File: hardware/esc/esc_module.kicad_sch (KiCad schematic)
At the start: 31 parts, among them U3 STDRIVE101, U4 STM32L431KBU6

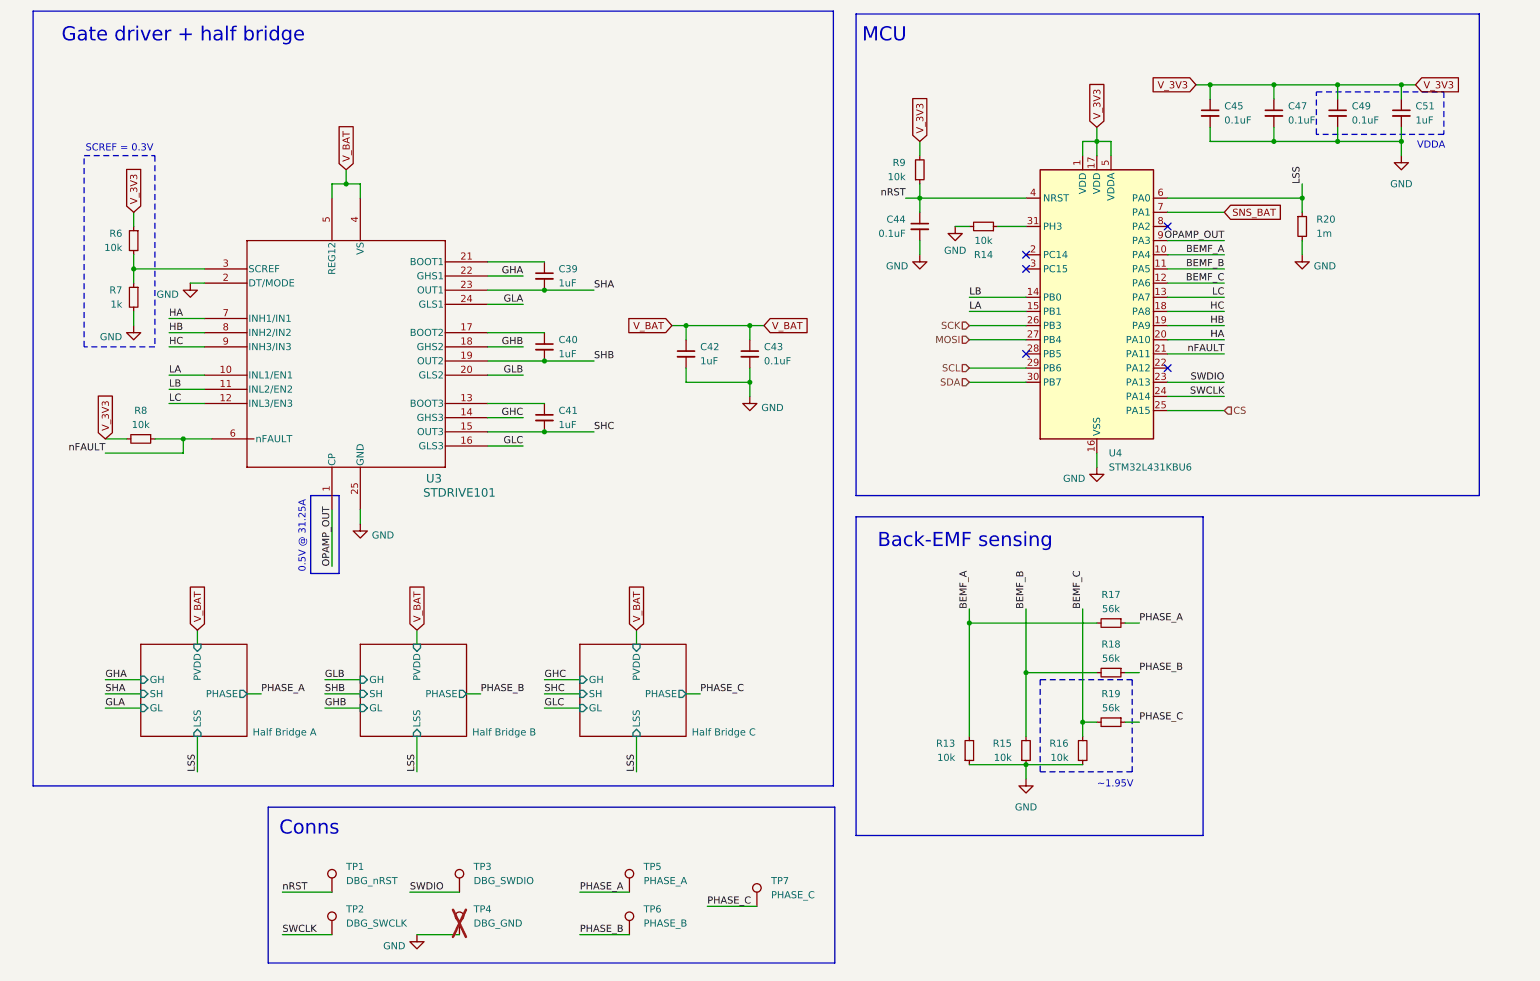
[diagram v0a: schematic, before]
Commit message: h/feat: preliminary rev 2 schematic
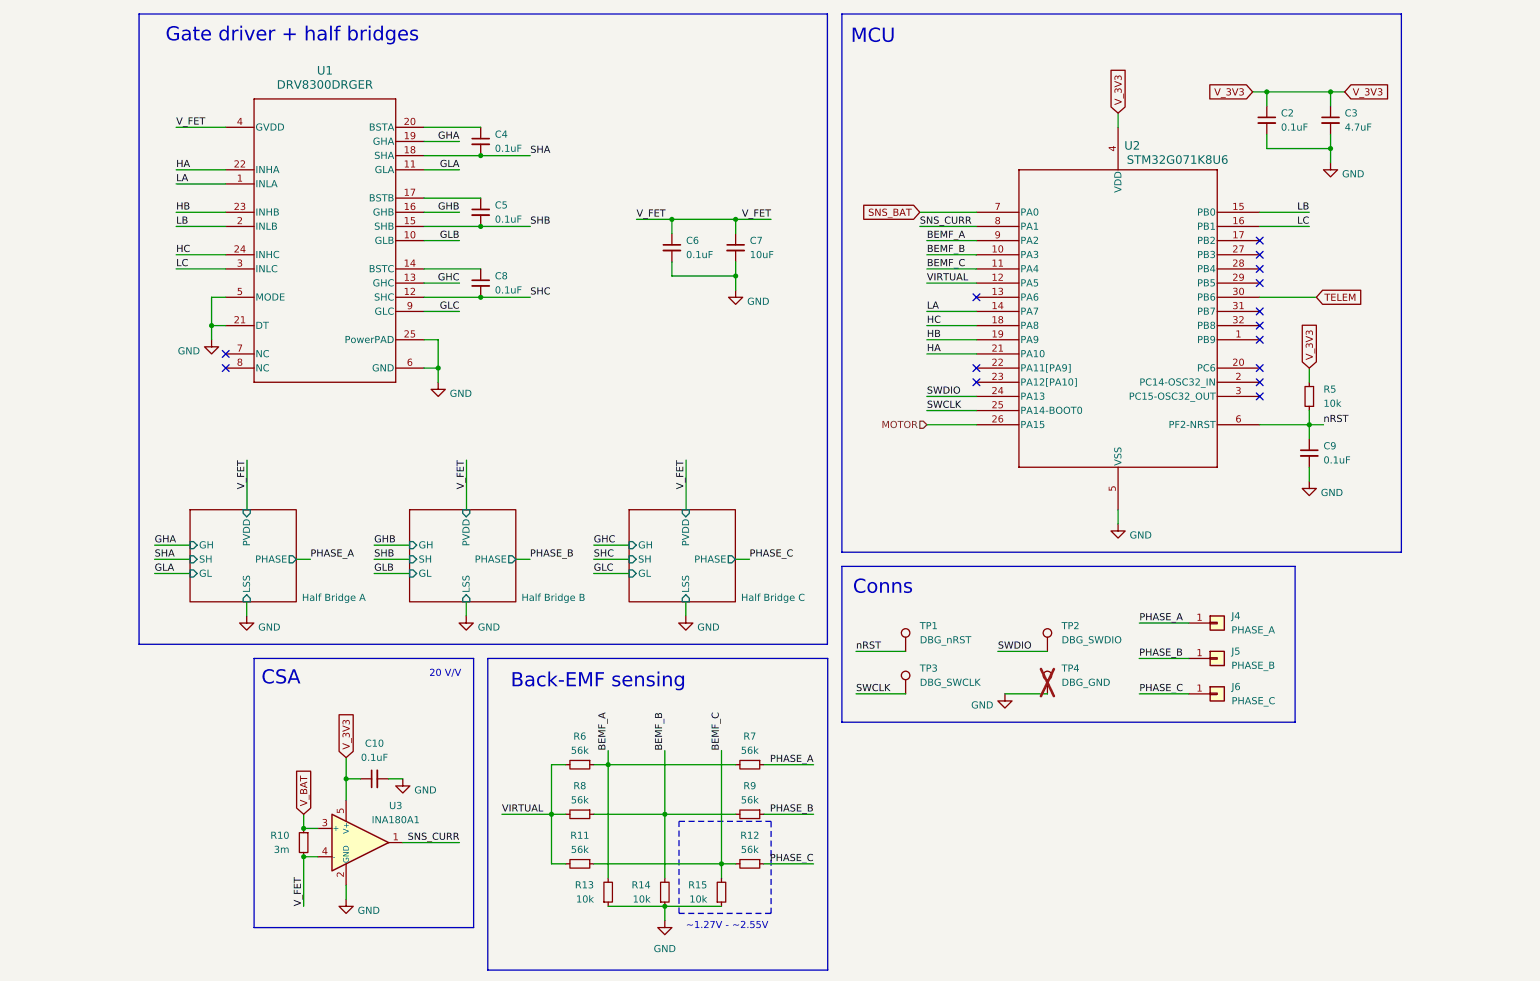
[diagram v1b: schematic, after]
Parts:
- removed C39, C40, C41, C51: 1uF, Capacitor_SMD:C_0402_1005Metric, symbol Device:C_Small
- removed C44, C45, C47, C49: 0.1uF, Capacitor_SMD:C_0402_1005Metric, symbol Device:C_Small
- removed R14, R9: 10k, Resistor_SMD:R_0402_1005Metric, symbol Device:R_Small
- removed R20: 1m, Resistor_SMD:R_0805_2012Metric, symbol Device:R_Small
- removed R7: 1k, Resistor_SMD:R_0402_1005Metric, symbol Device:R_Small
- removed TP5: PHASE_A, Stratus:Phase_Pad_3x3_D1.5, symbol Connector:TestPoint
- removed TP6: PHASE_B, Stratus:Phase_Pad_3x3_D1.5, symbol Connector:TestPoint
- removed TP7: PHASE_C, Stratus:Phase_Pad_3x3_D1.5, symbol Connector:TestPoint
- removed U3: STDRIVE101, Stratus:STDRIVE101, symbol STDRIVE101:STDRIVE101
- removed U4: STM32L431KBU6, Stratus:STM32L431KBU6, symbol MCU_ST_STM32L4:STM32L431KBUx
- added C10, C2, C4, C5, C8, C9: 0.1uF, Capacitor_SMD:C_0402_1005Metric, symbol Device:C_Small
- added C3: 4.7uF, Capacitor_SMD:C_0402_1005Metric, symbol Device:C_Small
- added J4: PHASE_A, Stratus:Phase_Pad_3x3_D1.5, symbol Connector_Generic:Conn_01x01
- added J5: PHASE_B, Stratus:Phase_Pad_3x3_D1.5, symbol Connector_Generic:Conn_01x01
- added J6: PHASE_C, Stratus:Phase_Pad_3x3_D1.5, symbol Connector_Generic:Conn_01x01
- added R10: 3m, Resistor_SMD:R_2512_6332Metric, symbol Device:R_Small
- added R11: 56k, Resistor_SMD:R_0402_1005Metric, symbol Device:R_Small
- added R5: 10k, Resistor_SMD:R_0402_1005Metric, symbol Device:R_Small
- added U1: DRV8300DRGER, DRV8300DRGER:DRV8300DRGER, symbol DRV8300DRGER:DRV8300DRGER
- added U2: STM32G071K8U6, STM32G071K8U6:STM32G071K8U6, symbol STM32G071K8U6:STM32G071K8U6
- added U3: INA180A1, Package_TO_SOT_SMD:SOT-23-5, symbol Amplifier_Current:INA180A1
- C6: renamed from C42; value 1uF -> 0.1uF
- C7: renamed from C43; value 0.1uF -> 10uF; footprint Capacitor_SMD:C_0402_1005Metric -> Capacitor_SMD:C_0805_2012Metric
- R6, R8: value 10k -> 56k; Manufacturer_Part_Number RC0402FR-0710KL -> RC0402FR-0756KL
- renumbered R19 to R12, R15 to R14, R16 to R15, R17 to R7, R18 to R9, TP3 to TP2, TP2 to TP3
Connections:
- net nFAULT is gone; now on net BEMF_B: R8.1
- net BEMF_A: now also R6.1, U2.9 (PA2)
- net BEMF_B: now also U2.10 (PA3)
- net BEMF_C: now also R11.1, U2.11 (PA4)
- net GHA: now also U1.19 (GHA)
- net GHB: now also U1.16 (GHB)
- net GHC: now also U1.13 (GHC)
- net GLA: now also U1.11 (GLA)
- net GLB: now also U1.10 (GLB)
- net GLC: now also U1.9 (GLC)
- net GND: now also C10.2, C2.2, C3.2, C9.2, U1.21 (DT), U1.25 (PowerPAD), U1.5 (MODE), U1.6 (GND), U2.5 (VSS), U3.2 (GND)
- net HA: now also U1.22 (INHA), U2.21 (PA10)
- net HB: now also U1.23 (INHB), U2.19 (PA9)
- net HC: now also U1.24 (INHC), U2.18 (PA8)
- net LA: now also U1.1 (INLA), U2.14 (PA7)
- net LB: now also U1.2 (INLB), U2.15 (PB0)
- net LC: now also U1.3 (INLC), U2.16 (PB1)
- net PHASE_A: now also J4.1 (Pin_1)
- net PHASE_B: now also J5.1 (Pin_1)
- net PHASE_C: now also J6.1 (Pin_1)
- net SHA: now also C4.2, U1.18 (SHA)
- net SHB: now also C5.2, U1.15 (SHB)
- net SHC: now also C8.2, U1.12 (SHC)
- net SNS_BAT: now also U2.7 (PA0)
- net SWCLK: now also U2.25 (PA14-BOOT0)
- net SWDIO: now also U2.24 (PA13)
- net V_3V3: now also C10.1, C2.1, C3.1, R5.2, U2.4 (VDD), U3.5 (V+); no longer R6.1, R8.2
- net V_BAT: now also R10.1, U3.3 (+); no longer C6.1, C7.1
- net nRST: now also C9.1, R5.1, U2.6 (PF2-NRST)
- net VIRTUAL: now reaches R6.2
- net VIRTUAL: now also R8.2, R11.2, U2.12 (PA5)
- new net: C8.1, U1.14 (BSTC)
- new net: C5.1, U1.17 (BSTB)
- new net: C4.1, U1.20 (BSTA)
- new net MOTOR: U2.26 (PA15)
- new net SNS_CURR: U2.8 (PA1), U3.1
- new net TELEM: U2.30 (PB6)
- new net V_FET: C6.1, C7.1, R10.2, U1.4 (GVDD), U3.4 (-)
- no-connect marks 5 -> 15
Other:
- note added: "20 V/V"
- note added: "CSA"
- note added: "Gate driver + half bridges"
- note added: "~1.27V - ~2.55V"
- note removed: "0.5V @ 31.25A"
- note removed: "Gate driver + half bridge"
- note removed: "SCREF = 0.3V"
- note removed: "VDDA"
- note removed: "~1.95V"
- moved on the sheet: C6, C7, R12, R13, R14, R15, R7, R9, TP1, TP2, TP3, TP4

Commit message: chore: prep: footprints, 3d models, pcb
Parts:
- U1: footprint DRV8300DRGER:DRV8300DRGER -> Stratus:DRV8300DRGER
- U2: footprint STM32G071K8U6:STM32G071K8U6 -> Stratus:STM32G071K8U6
- U3: footprint Package_TO_SOT_SMD:SOT-23-5 -> Stratus:INA180A1IDBVR
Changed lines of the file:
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@@
 			)
 		)
-		(property "Footprint" "DRV8300DRGER:DRV8300DRGER"
+		(property "Footprint" "Stratus:DRV8300DRGER"
 			(at 49.53 35.56 0)
 			(hide yes)
@@
 			)
 		)
-		(property "Footprint" "STM32G071K8U6:STM32G071K8U6"
+		(property "Footprint" "Stratus:STM32G071K8U6"
 			(at 184.15 50.8 0)
 			(hide yes)
@@
 			)
 		)
-		(property "Footprint" "Package_TO_SOT_SMD:SOT-23-5"
+		(property "Footprint" "Stratus:INA180A1IDBVR"
 			(at 73.66 185.42 0)
 			(hide yes)

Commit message: h/feat: gate drive routing + prelim layout
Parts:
- C10, C2, C3, C4, C5, C6, C8, C9: footprint Capacitor_SMD:C_0402_1005Metric -> Stratus:C_0402
- R11, R12, R13, R14, R15, R5, R6, R7, R8, R9: footprint Resistor_SMD:R_0402_1005Metric -> Stratus:R_0402
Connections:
- net LA: now also U2.16 (PB1); no longer U2.14 (PA7)
- net LC: now also U2.14 (PA7); no longer U2.16 (PB1)
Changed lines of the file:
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@@
 	(wire
 		(pts
+			(xy 53.34 95.25) (xy 53.34 104.14)
+		)
+		(stroke
+			(width 0)
+			(type default)
+		)
+	)
+	(wire
+		(pts
 			(xy 85.09 40.64) (xy 95.25 40.64)
 		)
@@
 	(wire
 		(pts
-			(xy 53.34 95.25) (xy 53.34 104.14)
-		)
-		(stroke
-			(width 0)
-			(type default)
-		)
-	)
-	(wire
-		(pts
 			(xy 85.09 55.88) (xy 91.44 55.88)
 		)
@@
 		)
 	)
-	(label "LA"
+	(label "LC"
 		(at 175.26 68.58 0)
 		(effects
@@
 		)
 	)
-	(label "LC"
+	(label "LA"
 		(at 243.84 53.34 180)
 		(effects
@@
 			)
 		)
-		(property "Footprint" "Resistor_SMD:R_0402_1005Metric"
+		(property "Footprint" "Stratus:R_0402"
 			(at 143.51 167.64 0)
 			(hide yes)
@@
 			)
 		)
-		(property "Footprint" "Capacitor_SMD:C_0402_1005Metric"
+		(property "Footprint" "Stratus:C_0402"
 			(at 243.84 93.98 0)
 			(hide yes)
@@
 			)
 		)
-		(property "Footprint" "Resistor_SMD:R_0402_1005Metric"
+		(property "Footprint" "Stratus:R_0402"
 			(at 118.11 172.72 0)
 			(hide yes)
@@
 			)
 		)
-		(property "Footprint" "Resistor_SMD:R_0402_1005Metric"
+		(property "Footprint" "Stratus:R_0402"
 			(at 138.43 172.72 0)
 			(hide yes)
@@
 			)
 		)
-		(property "Footprint" "Capacitor_SMD:C_0402_1005Metric"
+		(property "Footprint" "Stratus:C_0402"
 			(at 247.65 34.29 0)
 			(hide yes)
@@
 			)
 		)
-		(property "Footprint" "Resistor_SMD:R_0402_1005Metric"
+		(property "Footprint" "Stratus:R_0402"
 			(at 113.03 158.75 0)
 			(hide yes)
@@
 			)
 		)
-		(property "Footprint" "Resistor_SMD:R_0402_1005Metric"
+		(property "Footprint" "Stratus:R_0402"
 			(at 113.03 149.86 0)
 			(hide yes)
@@
 			)
 		)
-		(property "Footprint" "Capacitor_SMD:C_0402_1005Metric"
+		(property "Footprint" "Stratus:C_0402"
 			(at 129.54 57.15 0)
 			(hide yes)
@@
 			)
 		)
-		(property "Footprint" "Capacitor_SMD:C_0402_1005Metric"
+		(property "Footprint" "Stratus:C_0402"
 			(at 95.25 63.5 0)
 			(hide yes)
@@
 			)
 		)
-		(property "Footprint" "Resistor_SMD:R_0402_1005Metric"
+		(property "Footprint" "Stratus:R_0402"
 			(at 143.51 158.75 0)
 			(hide yes)
@@
 			)
 		)
-		(property "Footprint" "Resistor_SMD:R_0402_1005Metric"
+		(property "Footprint" "Stratus:R_0402"
 			(at 113.03 167.64 0)
 			(hide yes)
@@
 			)
 		)
-		(property "Footprint" "Resistor_SMD:R_0402_1005Metric"
+		(property "Footprint" "Stratus:R_0402"
 			(at 128.27 172.72 0)
 			(hide yes)
@@
 			)
 		)
-		(property "Footprint" "Capacitor_SMD:C_0402_1005Metric"
+		(property "Footprint" "Stratus:C_0402"
 			(at 95.25 50.8 0)
 			(hide yes)
@@
 			)
 		)
-		(property "Footprint" "Capacitor_SMD:C_0402_1005Metric"
+		(property "Footprint" "Stratus:C_0402"
 			(at 76.2 152.4 0)
 			(hide yes)
@@
 			)
 		)
-		(property "Footprint" "Capacitor_SMD:C_0402_1005Metric"
+		(property "Footprint" "Stratus:C_0402"
 			(at 95.25 38.1 0)
 			(hide yes)
@@
 			)
 		)
-		(property "Footprint" "Resistor_SMD:R_0402_1005Metric"
+		(property "Footprint" "Stratus:R_0402"
 			(at 143.51 149.86 0)
 			(hide yes)
@@
 			)
 		)
-		(property "Footprint" "Resistor_SMD:R_0402_1005Metric"
+		(property "Footprint" "Stratus:R_0402"
 			(at 243.84 83.82 0)
 			(hide yes)
@@
 			)
 		)
-		(property "Footprint" "Capacitor_SMD:C_0402_1005Metric"
+		(property "Footprint" "Stratus:C_0402"
 			(at 236.22 34.29 0)
 			(hide yes)
@@
 		)
 		(pin "PVDD" input
-			(at 53.2878 104.14 90)
+			(at 53.34 104.14 90)
 			(effects
 				(font
@@
 		)
 		(pin "PVDD" input
-			(at 132.0278 104.14 90)
+			(at 132.08 104.14 90)
 			(effects
 				(font
@@
 		)
 		(pin "PVDD" input
-			(at 92.6578 104.14 90)
+			(at 92.71 104.14 90)
 			(effects
 				(font

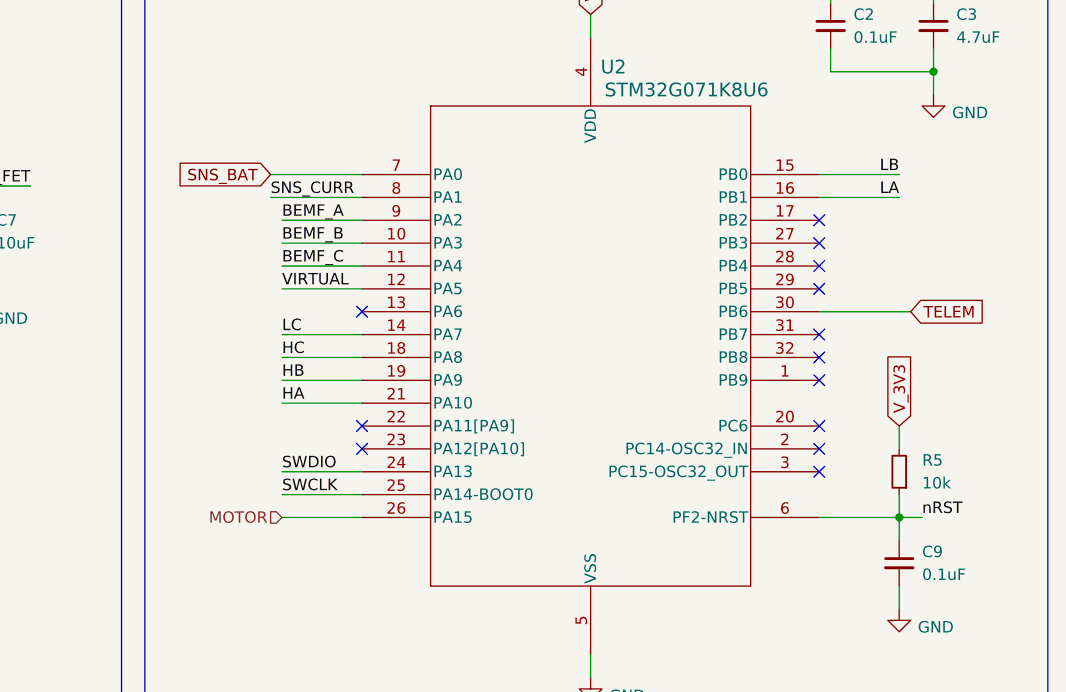
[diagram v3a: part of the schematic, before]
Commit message: h/fix: update schematic to better match AM32 hardware groups; further layout work
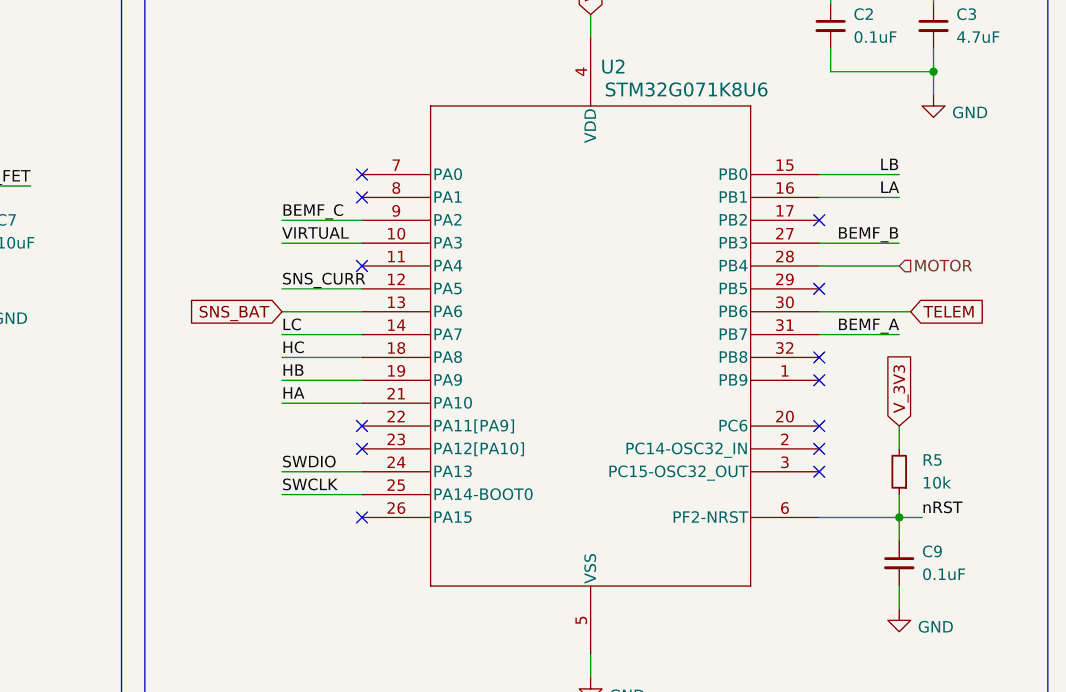
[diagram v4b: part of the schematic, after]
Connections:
- net BEMF_A: now also U2.31 (PB7); no longer U2.9 (PA2)
- net BEMF_B: now also U2.27 (PB3); no longer U2.10 (PA3)
- net BEMF_C: now also U2.9 (PA2); no longer U2.11 (PA4)
- net MOTOR: now also U2.28 (PB4); no longer U2.26 (PA15)
- net SNS_BAT: now also U2.13 (PA6); no longer U2.7 (PA0)
- net SNS_CURR: now also U2.12 (PA5); no longer U2.8 (PA1)
- net VIRTUAL: now also U2.10 (PA3); no longer U2.12 (PA5)
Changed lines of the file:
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@@
-	)
-	(no_connect
-		(at 234.95 58.42)
-	)
-	(no_connect
-		(at 184.15 66.04)
 	)
 	(no_connect
@@
 	)
 	(no_connect
+		(at 184.15 88.9)
+	)
+	(no_connect
+		(at 184.15 50.8)
+	)
+	(no_connect
 		(at 234.95 63.5)
 	)
@@
 	)
 	(no_connect
+		(at 184.15 53.34)
+	)
+	(no_connect
 		(at 184.15 81.28)
 	)
@@
 	)
 	(no_connect
-		(at 234.95 60.96)
-	)
-	(no_connect
 		(at 49.53 76.2)
 	)
@@
 	)
 	(no_connect
-		(at 234.95 68.58)
+		(at 184.15 60.96)
 	)
 	(no_connect
@@
 	(wire
 		(pts
+			(xy 175.26 66.04) (xy 184.15 66.04)
+		)
+		(stroke
+			(width 0)
+			(type default)
+		)
+	)
+	(wire
+		(pts
 			(xy 236.22 29.21) (xy 233.68 29.21)
 		)
@@
 	(wire
 		(pts
-			(xy 184.15 50.8) (xy 173.99 50.8)
-		)
-		(stroke
-			(width 0)
-			(type default)
-		)
-	)
-	(wire
-		(pts
 			(xy 53.2878 120.65) (xy 53.2878 123.19)
 		)
@@
 	(wire
 		(pts
-			(xy 184.15 53.34) (xy 173.99 53.34)
-		)
-		(stroke
-			(width 0)
-			(type default)
-		)
-	)
-	(wire
-		(pts
 			(xy 63.5 166.37) (xy 66.04 166.37)
 		)
@@
 	(wire
 		(pts
+			(xy 234.95 68.58) (xy 243.84 68.58)
+		)
+		(stroke
+			(width 0)
+			(type default)
+		)
+	)
+	(wire
+		(pts
 			(xy 40.64 45.72) (xy 49.53 45.72)
 		)
@@
 	(wire
 		(pts
+			(xy 234.95 58.42) (xy 243.84 58.42)
+		)
+		(stroke
+			(width 0)
+			(type default)
+		)
+	)
+	(wire
+		(pts
 			(xy 85.09 50.8) (xy 91.44 50.8)
 		)
@@
 	(wire
 		(pts
-			(xy 184.15 88.9) (xy 175.26 88.9)
-		)
-		(stroke
-			(width 0)
-			(type default)
-		)
-	)
-	(wire
-		(pts
 			(xy 99.06 158.75) (xy 107.95 158.75)
 		)
@@
 	(wire
 		(pts
+			(xy 234.95 60.96) (xy 243.84 60.96)
+		)
+		(stroke
+			(width 0)
+			(type default)
+		)
+	)
+	(wire
+		(pts
 			(xy 140.97 64.77) (xy 140.97 62.23)
-		)
-		(stroke
-			(width 0)
-			(type default)
-		)
-	)
-	(wire
-		(pts
-			(xy 184.15 60.96) (xy 175.26 60.96)
 		)
 		(stroke
@@
 		)
 	)
+	(label "BEMF_A"
+		(at 243.84 68.58 180)
+		(effects
+			(font
+				(size 1.27 1.27)
+			)
+			(justify right bottom)
+		)
+	)
 	(label "PHASE_B"
 		(at 104.0878 113.03 0)
@@
 		)
 	)
+	(label "BEMF_B"
+		(at 243.84 58.42 180)
+		(effects
+			(font
+				(size 1.27 1.27)
+			)
+			(justify right bottom)
+		)
+	)
 	(label "GHC"
 		(at 91.44 63.5 180)
@@
 		)
 	)
-	(label "BEMF_A"
+	(label "BEMF_C"
 		(at 175.26 55.88 0)
 		(effects
@@
 		)
 	)
-	(label "SNS_CURR"
-		(at 173.99 53.34 0)
-		(effects
-			(font
-				(size 1.27 1.27)
-			)
-			(justify left bottom)
-		)
-	)
 	(label "HA"
 		(at 175.26 76.2 0)
@@
 		)
 	)
-	(label "BEMF_B"
+	(label "VIRTUAL"
 		(at 175.26 58.42 0)
 		(effects
@@
 		)
 	)
-	(label "VIRTUAL"
+	(label "SNS_CURR"
 		(at 175.26 63.5 0)
 		(effects
@@
 	(label "SWCLK"
 		(at 175.26 86.36 0)
-		(effects
-			(font
-				(size 1.27 1.27)
-			)
-			(justify left bottom)
-		)
-	)
-	(label "BEMF_C"
-		(at 175.26 60.96 0)
 		(effects
 			(font
@@
 	(global_label "SNS_BAT"
 		(shape input)
-		(at 173.99 50.8 180)
+		(at 175.26 66.04 180)
 		(fields_autoplaced yes)
 		(effects
@@
 		)
 		(property "Intersheetrefs" "${INTERSHEET_REFS}"
-			(at 162.9615 50.8 0)
+			(at 164.2315 66.04 0)
 			(hide yes)
 			(show_name no)
@@
 	(hierarchical_label "MOTOR"
 		(shape input)
-		(at 175.26 88.9 180)
-		(effects
-			(font
-				(size 1.27 1.27)
-			)
-			(justify right)
-		)
-	)
+		(at 243.84 60.96 0)
+		(effects
+			(font
+				(size 1.27 1.27)
+			)
+			(justify left)
+		)
+	)

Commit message: h/feat: layout - 1/4 motors
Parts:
- added C59, C60, C64: 10uF, Capacitor_SMD:C_0805_2012Metric, symbol Device:C_Small
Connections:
- net GND: now also C59.2, C60.2, C64.2
- net V_FET: now also C59.1, C60.1, C64.1
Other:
- note added: "10uF * 3"
- note added: "MLCCs"
